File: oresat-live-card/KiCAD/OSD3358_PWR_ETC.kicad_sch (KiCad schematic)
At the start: 30 parts, among them Q1 MMBT2907, U10 TLVH431, U4 SN74LVC1G07DCK, U7 OSD3358-512M-BSM

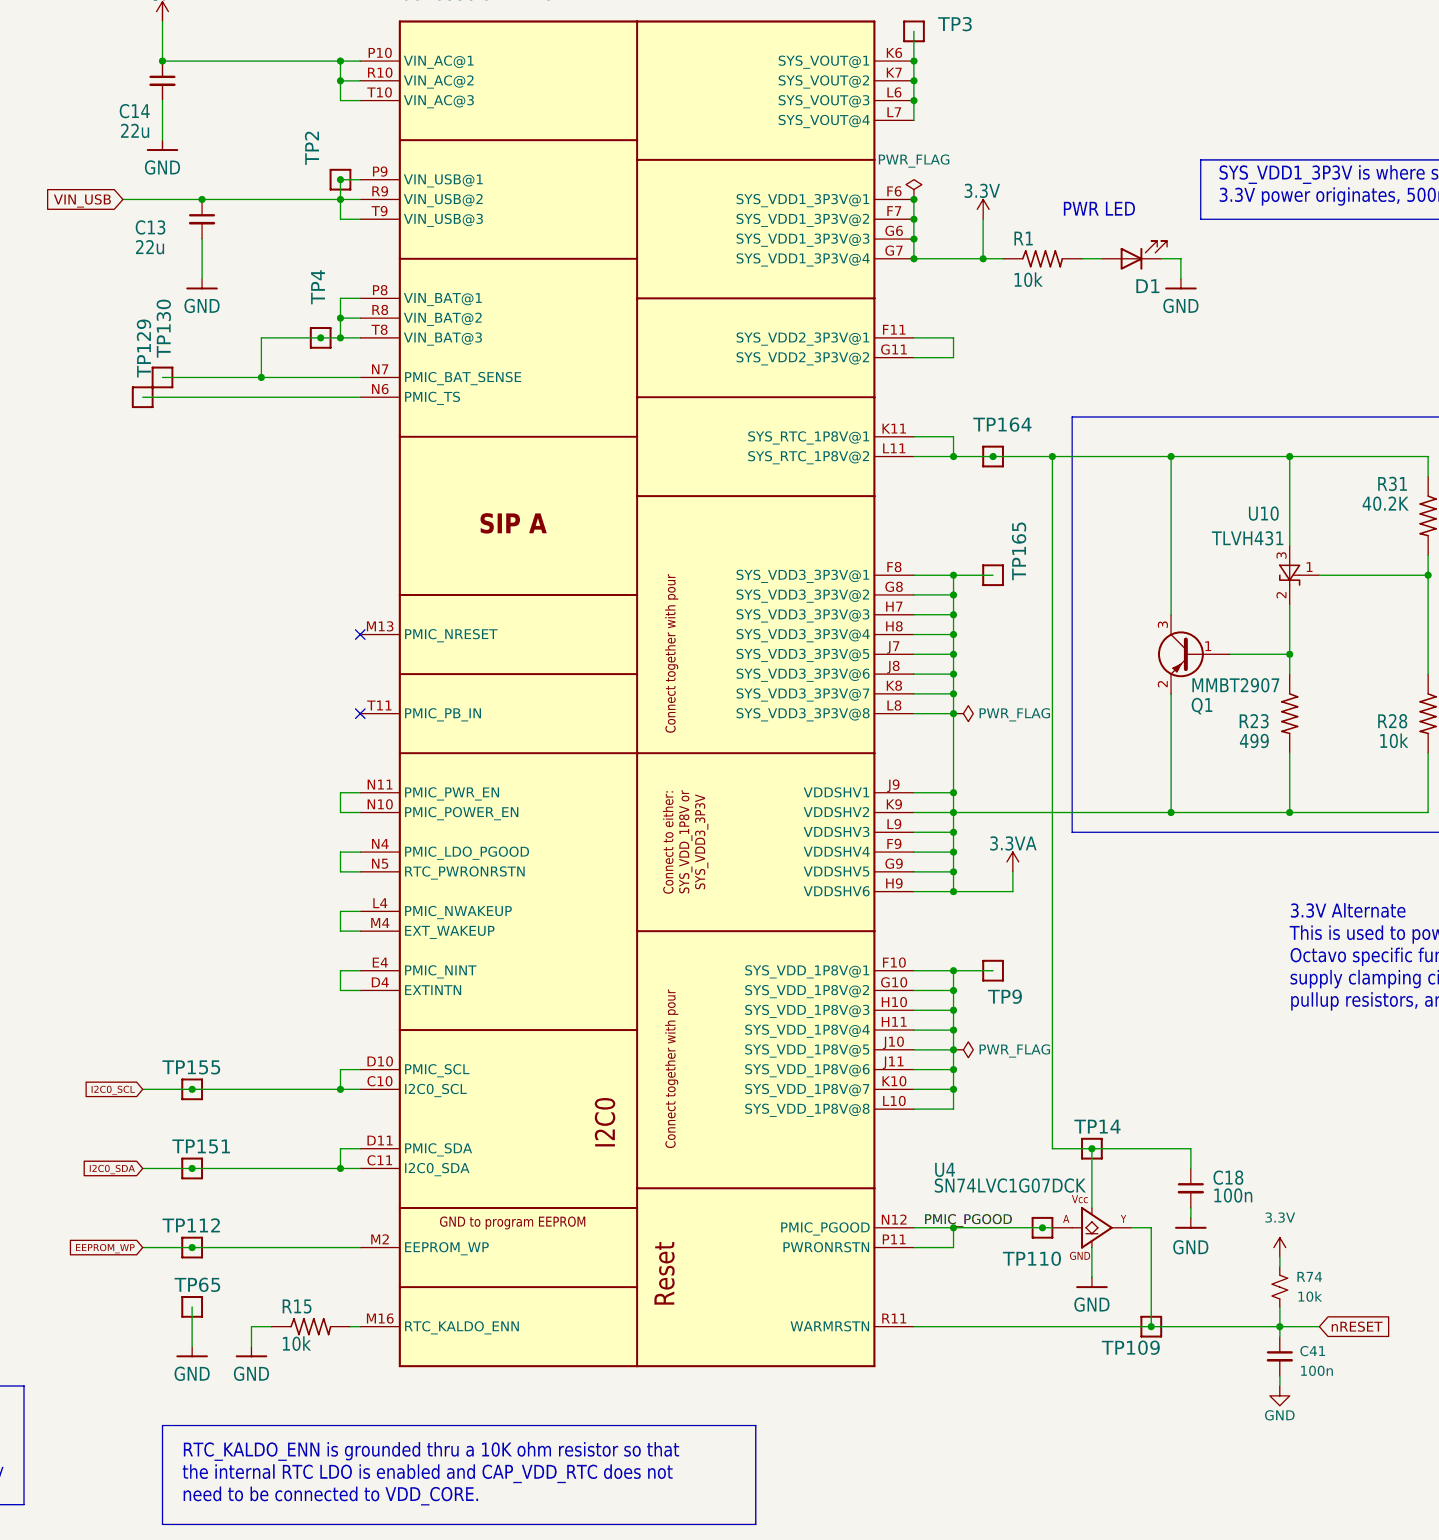
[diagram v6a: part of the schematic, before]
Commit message: completed tx/rx switch circuit and cleaned up GND references
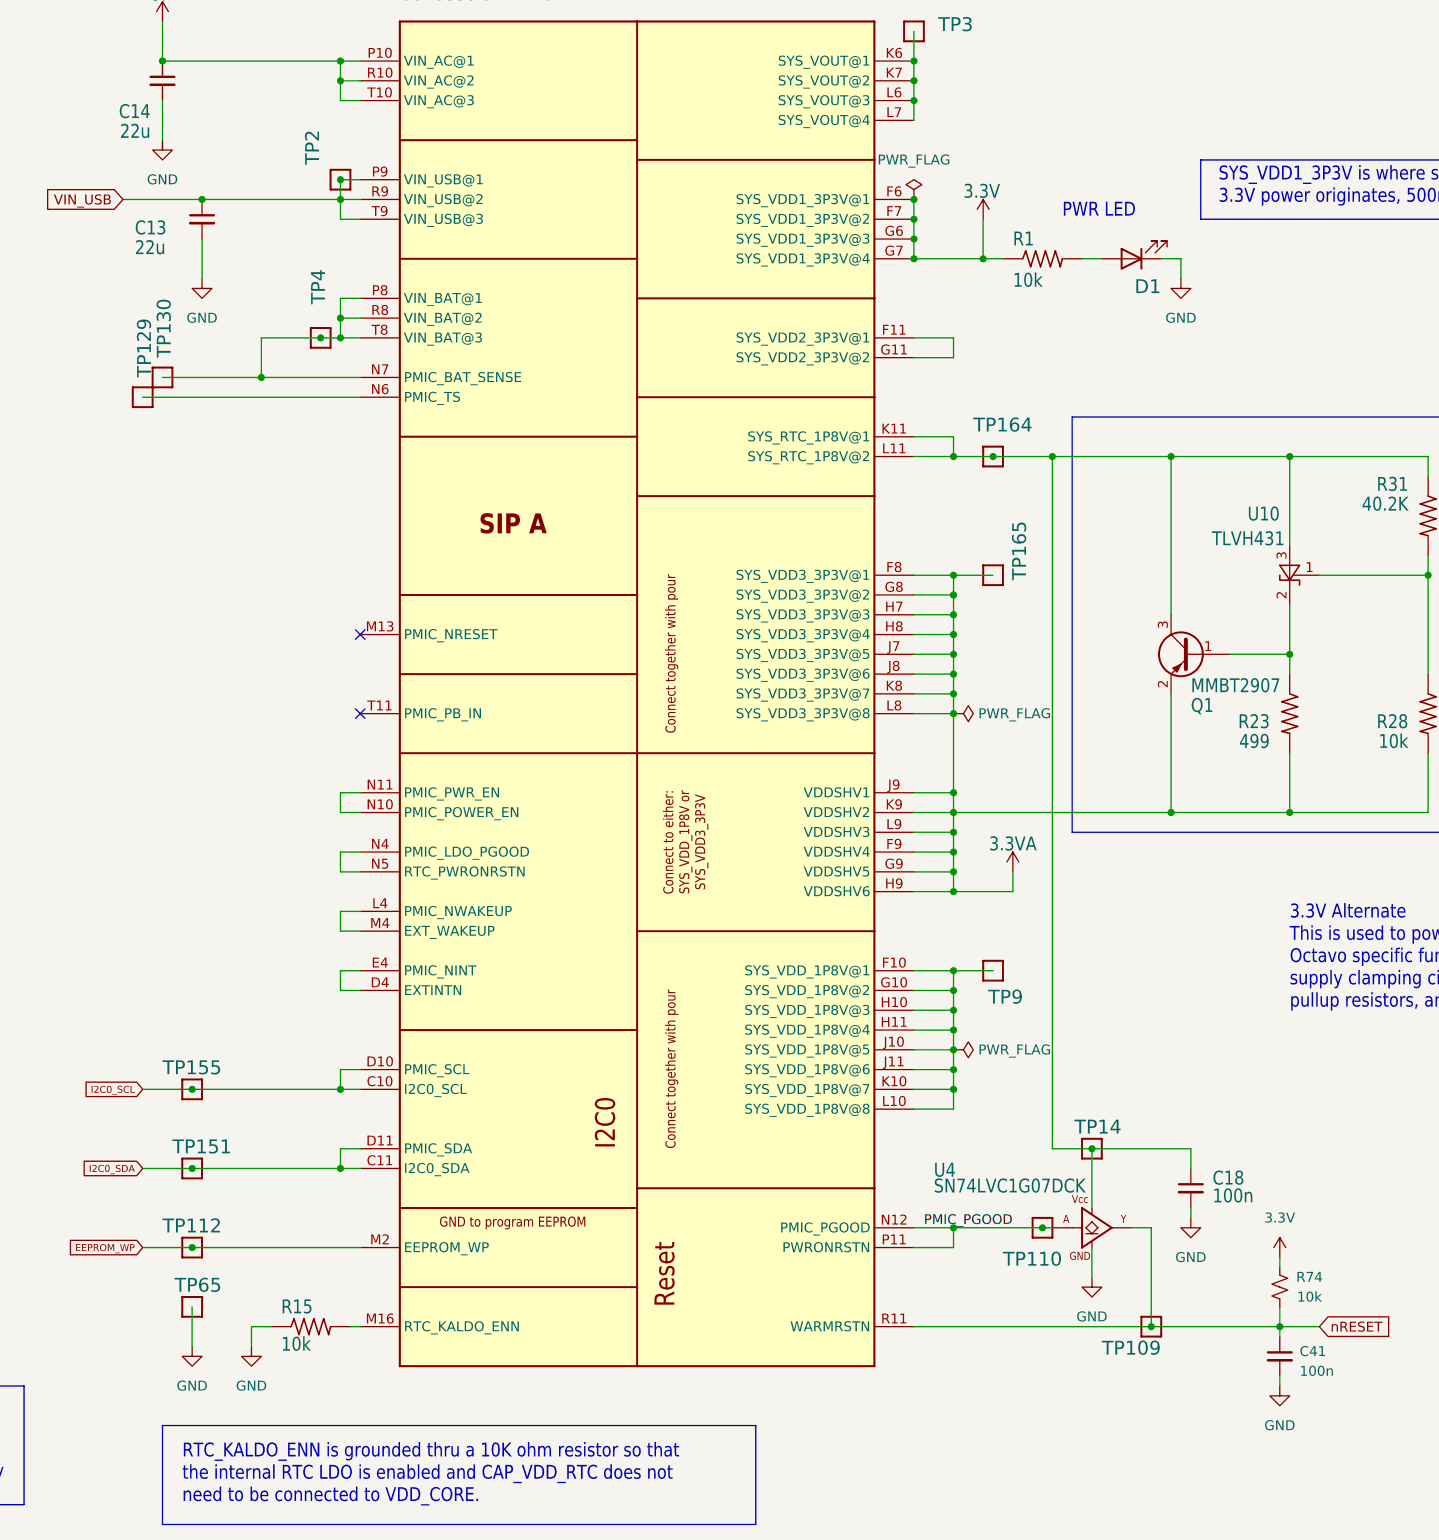
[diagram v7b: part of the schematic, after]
